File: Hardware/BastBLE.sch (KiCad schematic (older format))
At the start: 33 parts

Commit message: assigned pinout complete
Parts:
- U2: renamed from U?; symbol electroniccats:E73-2G4M08S1C -> BastBLE-rescue:E73-2G4M08S1C-electroniccats
- gave numbers to parts that had none: 32
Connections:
- net labels removed: BOOT, DFU, SWDCLK
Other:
- note added: "NOTA: BOOT"
- note added: "NOTA: DFU??"

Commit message: SWD pinout ok, assigned mosfet
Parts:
- removed Q1: BS870, Package_TO_SOT_SMD:SOT-23, symbol Transistor_FET:BS870
- added Q?: DMG3415U-7, symbol Device:Q_PMOS_SGD
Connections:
- wire segments 173 -> 172
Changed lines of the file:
@@
-$EndComp
-$Comp
-L Transistor_FET:BS870 Q1
-U 1 1 5E1F28D4
-P 1190 5640
-F 0 "Q1" H 1396 5686 50  0000 L CNN
-F 1 "BS870" H 1396 5595 50  0000 L CNN
-F 2 "Package_TO_SOT_SMD:SOT-23" H 1390 5565 50  0001 L CIN
-F 3 "http://www.diodes.com/assets/Datasheets/ds11302.pdf" H 1190 5640 50  0001 L CNN
-	1    1190 5640
-	1    0    0    -1
 $EndComp
 $Comp
@@
 Wire Wire Line
 	6190 5690 6120 5690
+Text Label 6115 5490 2    50   ~ 0
+SWDIO
 Text Label 6120 5590 2    50   ~ 0
-SWDIO
-Text Label 6120 5690 2    50   ~ 0
 SWCLK
 $Comp
 L power:GND #PWR029
 U 1 1 5E237980
-P 5810 5565
-F 0 "#PWR029" H 5810 5315 50  0001 C CNN
-F 1 "GND" H 5815 5392 50  0000 C CNN
-F 2 "" H 5810 5565 50  0001 C CNN
-F 3 "" H 5810 5565 50  0001 C CNN
-	1    5810 5565
+P 6120 5690
+F 0 "#PWR029" H 6120 5440 50  0001 C CNN
+F 1 "GND" H 6125 5517 50  0000 C CNN
+F 2 "" H 6120 5690 50  0001 C CNN
+F 3 "" H 6120 5690 50  0001 C CNN
+	1    6120 5690
 	1    0    0    -1
 $EndComp
@@
 	1    0    0    -1
 $EndComp
-Wire Wire Line
-	5810 5490 5810 5565
-Wire Wire Line
-	5810 5490 6190 5490
 Wire Notes Line
 	6975 6530 6975 4335
@@
 Text Notes 1195 3160 0    50   ~ 0
 NOTA: BOOT
+Wire Wire Line
+	6190 5490 6115 5490
+$Comp
+L Device:Q_PMOS_SGD Q?
+U 1 1 5E39C807
+P 1190 5640
+F 0 "Q?" H 1394 5686 50  0000 L CNN
+F 1 "DMG3415U-7" H 1370 5770 50  0000 L CNN
+F 2 "" H 1390 5740 50  0001 C CNN
+F 3 "~" H 1190 5640 50  0001 C CNN
+	1    1190 5640
+	1    0    0    -1
+$EndComp
 $EndSCHEMATC

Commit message: Format adafruit in PCB, init BOM
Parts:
- C1, C2, C3, C4, C5, C6, C7, C8: footprint (none) -> Capacitor_SMD:C_0603_1608Metric_Pad1.05x0.95mm_HandSolder
- D1: footprint Diode_THT:D_DO-201AD_P15.24mm_Horizontal -> Diode_SMD:D_SOD-123F
- D2, D3: footprint (none) -> LED_SMD:LED_0603_1608Metric_Pad1.05x0.95mm_HandSolder
- R1, R2, R3, R4, R5, R6, R7, R8, R9: footprint (none) -> Resistor_SMD:R_0603_1608Metric_Pad1.05x0.95mm_HandSolder
- gave numbers to parts that had none: 1
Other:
- moved on the sheet: J4, L1, Y1

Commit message: init assignament footprints
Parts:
- J2: footprint (none) -> Connector_PinSocket_2.54mm:PinSocket_1x04_P2.54mm_Vertical
- J3: footprint (none) -> Connector_PinHeader_2.54mm:PinHeader_1x16_P2.54mm_Vertical
- J4: footprint (none) -> Connector_PinHeader_2.54mm:PinHeader_1x12_P2.54mm_Vertical
- L1: footprint (none) -> Connector_PinHeader_2.54mm:PinHeader_2x01_P2.54mm_Vertical_SMD
- P1: footprint (none) -> Connectors_ElectronicCats:C393939
- Q1: footprint (none) -> Package_TO_SOT_SMD:SOT-23_Handsoldering
- SW1: footprint (none) -> Button_Switch_SMD:SW_SPST_TL3342
- U2: footprint (none) -> Rf:E73-2G4M08S1C-52840
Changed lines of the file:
@@
 F 0 "U2" H 2220 3290 50  0000 C CNN
 F 1 "E73-2G4M08S1C" H 2220 3199 50  0000 C CNN
-F 2 "" H 2245 1925 50  0001 C CNN
+F 2 "Rf:E73-2G4M08S1C-52840" H 2245 1925 50  0001 C CNN
 F 3 "" H 2245 1925 50  0001 C CNN
 	1    2245 1925
@@
 F 0 "L1" V 3165 2605 50  0000 C CNN
 F 1 "10uH" V 3070 2735 50  0000 C CNN
-F 2 "" H 3120 2725 50  0001 C CNN
+F 2 "Connector_PinHeader_2.54mm:PinHeader_2x01_P2.54mm_Vertical_SMD" H 3120 2725 50  0001 C CNN
 F 3 "~" H 3120 2725 50  0001 C CNN
 	1    3120 2725
@@
 F 0 "J4" H 10000 1902 50  0000 L CNN
 F 1 "Conn_right" V 10035 1390 50  0000 L CNN
-F 2 "" H 9920 1910 50  0001 C CNN
+F 2 "Connector_PinHeader_2.54mm:PinHeader_1x12_P2.54mm_Vertical" H 9920 1910 50  0001 C CNN
 F 3 "~" H 9920 1910 50  0001 C CNN
 	1    9920 1910
@@
 F 0 "J3" H 9223 1090 50  0000 C CNN
 F 1 "Conn_left" V 9410 2125 50  0000 C CNN
-F 2 "" H 9305 2115 50  0001 C CNN
+F 2 "Connector_PinHeader_2.54mm:PinHeader_1x16_P2.54mm_Vertical" H 9305 2115 50  0001 C CNN
 F 3 "~" H 9305 2115 50  0001 C CNN
 	1    9305 2115
@@
 F 0 "P1" H 5242 3987 50  0000 C CNN
 F 1 "USB_C_Plug_USB2.0" H 5242 3896 50  0000 C CNN
-F 2 "" H 5285 3120 50  0001 C CNN
+F 2 "Connectors_ElectronicCats:C393939" H 5285 3120 50  0001 C CNN
 F 3 "https://www.usb.org/sites/default/files/documents/usb_type-c.zip" H 5285 3120 50  0001 C CNN
 	1    5135 3120
@@
 F 0 "SW1" H 7380 1380 50  0000 C CNN
 F 1 "RESET" H 7380 1289 50  0000 C CNN
-F 2 "" H 7380 1295 50  0001 C CNN
-F 3 "~" H 7380 1295 50  0001 C CNN
+F 2 "Button_Switch_SMD:SW_SPST_TL3342" H 7380 1295 50  0001 C CNN
+F 3 "TS-1185EC-C-D-B" H 7380 1295 50  0001 C CNN
 	1    7380 1095
 	1    0    0    -1
@@
 F 0 "J2" H 6470 5482 50  0000 L CNN
 F 1 "SWD" H 6470 5391 50  0000 L CNN
-F 2 "" H 6390 5490 50  0001 C CNN
+F 2 "Connector_PinSocket_2.54mm:PinSocket_1x04_P2.54mm_Vertical" H 6390 5490 50  0001 C CNN
 F 3 "~" H 6390 5490 50  0001 C CNN
 	1    6390 5490
@@
 F 0 "Q1" H 1394 5686 50  0000 L CNN
 F 1 "DMG3415U-7" H 1370 5770 50  0000 L CNN
-F 2 "" H 1390 5740 50  0001 C CNN
+F 2 "Package_TO_SOT_SMD:SOT-23_Handsoldering" H 1390 5740 50  0001 C CNN
 F 3 "~" H 1190 5640 50  0001 C CNN
 	1    1190 5640

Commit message: Review PCB
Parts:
- U2: symbol BastBLE-rescue:E73-2G4M08S1C-electroniccats -> BastBLE-rescue:E73-2G4M08S1C-electroniccats-BastBLE-rescue
- Y1: footprint (none) -> Crystal:Crystal_SMD_SeikoEpson_MC146-4Pin_6.7x1.5mm
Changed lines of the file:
@@
 $EndDescr
 $Comp
-L BastBLE-rescue:E73-2G4M08S1C-electroniccats U2
+L BastBLE-rescue:E73-2G4M08S1C-electroniccats-BastBLE-rescue U2
 U 1 1 5E1E9971
 P 2245 1925
@@
 F 3 "" H 2245 1925 50  0001 C CNN
 	1    2245 1925
-	1    0    0    -1
-$EndComp
-$Comp
-L Battery_Management:MCP73831-2-OT U3
-U 1 1 5E1EEE26
-P 4270 5305
-F 0 "U3" H 4385 5550 50  0000 C CNN
-F 1 "MCP73831-2-OT" H 3880 5545 50  0000 C CNN
-F 2 "Package_TO_SOT_SMD:SOT-23-5" H 4320 5055 50  0001 L CIN
-F 3 "http://ww1.microchip.com/downloads/en/DeviceDoc/20001984g.pdf" H 4120 5255 50  0001 C CNN
-	1    4270 5305
 	1    0    0    -1
 $EndComp
@@
 F 0 "Y1" V 1110 1730 50  0000 L CNN
 F 1 "32Khz" V 1195 1650 50  0000 L CNN
-F 2 "" H 1200 1955 50  0001 C CNN
+F 2 "Crystal:Crystal_SMD_SeikoEpson_MC146-4Pin_6.7x1.5mm" H 1200 1955 50  0001 C CNN
 F 3 "~" H 1200 1955 50  0001 C CNN
 	1    1200 1955
@@
 $EndComp
 Wire Wire Line
-	4270 5005 4270 4920
-Wire Wire Line
-	4270 5605 4270 5640
-$Comp
-L power:GND #PWR017
-U 1 1 5E25A527
-P 4270 5675
-F 0 "#PWR017" H 4270 5425 50  0001 C CNN
-F 1 "GND" H 4275 5502 50  0000 C CNN
-F 2 "" H 4270 5675 50  0001 C CNN
-F 3 "" H 4270 5675 50  0001 C CNN
-	1    4270 5675
-	1    0    0    -1
-$EndComp
-Wire Wire Line
-	4670 5205 4745 5205
-Wire Wire Line
-	4670 5405 4740 5405
-Wire Wire Line
-	3870 5405 3745 5405
-$Comp
-L Device:LED D3
-U 1 1 5E2607F0
-P 5185 5405
-F 0 "D3" H 5178 5621 50  0000 C CNN
-F 1 "LED" H 5178 5530 50  0000 C CNN
-F 2 "LED_SMD:LED_0603_1608Metric_Pad1.05x0.95mm_HandSolder" H 5185 5405 50  0001 C CNN
-F 3 "~" H 5185 5405 50  0001 C CNN
-	1    5185 5405
-	1    0    0    -1
-$EndComp
-$Comp
-L Device:R_Small R7
-U 1 1 5E260E7D
-P 4840 5405
-F 0 "R7" V 4765 5405 50  0000 C CNN
-F 1 "1K" V 4920 5400 50  0000 C CNN
-F 2 "Resistor_SMD:R_0603_1608Metric_Pad1.05x0.95mm_HandSolder" H 4840 5405 50  0001 C CNN
-F 3 "~" H 4840 5405 50  0001 C CNN
-	1    4840 5405
-	0    1    1    0
-$EndComp
-Wire Wire Line
-	4940 5405 5035 5405
-Wire Wire Line
-	5335 5405 5415 5405
-Wire Wire Line
 	5415 5405 5415 5375
-$Comp
-L power:+BATT #PWR022
-U 1 1 5E26906E
-P 4915 5205
-F 0 "#PWR022" H 4915 5055 50  0001 C CNN
-F 1 "+BATT" H 4930 5378 50  0000 C CNN
-F 2 "" H 4915 5205 50  0001 C CNN
-F 3 "" H 4915 5205 50  0001 C CNN
-	1    4915 5205
-	1    0    0    -1
-$EndComp
-$Comp
-L Device:R_Small R3
-U 1 1 5E26C7D7
-P 3745 5505
-F 0 "R3" H 3804 5551 50  0000 L CNN
-F 1 "4K7" H 3804 5460 50  0000 L CNN
-F 2 "Resistor_SMD:R_0603_1608Metric_Pad1.05x0.95mm_HandSolder" H 3745 5505 50  0001 C CNN
-F 3 "~" H 3745 5505 50  0001 C CNN
-	1    3745 5505
-	1    0    0    -1
-$EndComp
-Wire Wire Line
-	3745 5605 3745 5640
-Wire Wire Line
-	3745 5640 4270 5640
-Connection ~ 4270 5640
-Wire Wire Line
-	4270 5640 4270 5675
-$Comp
-L Device:C_Small C3
-U 1 1 5E26FE7B
-P 4745 5035
-F 0 "C3" H 4610 5165 50  0000 L CNN
-F 1 "10uF" H 4510 5100 50  0000 L CNN
-F 2 "Capacitor_SMD:C_0603_1608Metric_Pad1.05x0.95mm_HandSolder" H 4745 5035 50  0001 C CNN
-F 3 "~" H 4745 5035 50  0001 C CNN
-	1    4745 5035
-	1    0    0    -1
-$EndComp
-Wire Wire Line
-	4745 5135 4745 5205
-Connection ~ 4745 5205
-Wire Wire Line
-	4745 5205 4915 5205
-Wire Wire Line
-	4745 4935 4745 4635
 Wire Wire Line
 	4745 4635 4830 4635
-Wire Wire Line
-	4830 4635 4830 4675
-$Comp
-L power:GND #PWR021
-U 1 1 5E275216
-P 4830 4675
-F 0 "#PWR021" H 4830 4425 50  0001 C CNN
-F 1 "GND" H 4835 4502 50  0000 C CNN
-F 2 "" H 4830 4675 50  0001 C CNN
-F 3 "" H 4830 4675 50  0001 C CNN
-	1    4830 4675
-	1    0    0    -1
-$EndComp
 $Comp
 L Connector:Screw_Terminal_01x02 J1
@@
 EN
 $Comp
-L power:VBUS #PWR016
-U 1 1 5E3A4B4E
-P 4270 4920
-F 0 "#PWR016" H 4270 4770 50  0001 C CNN
-F 1 "VBUS" H 4285 5093 50  0000 C CNN
-F 2 "" H 4270 4920 50  0001 C CNN
-F 3 "" H 4270 4920 50  0001 C CNN
-	1    4270 4920
-	1    0    0    -1
-$EndComp
-$Comp
-L power:VBUS #PWR026
-U 1 1 5E3A5E21
-P 5415 5375
-F 0 "#PWR026" H 5415 5225 50  0001 C CNN
-F 1 "VBUS" H 5430 5548 50  0000 C CNN
-F 2 "" H 5415 5375 50  0001 C CNN
-F 3 "" H 5415 5375 50  0001 C CNN
-	1    5415 5375
-	1    0    0    -1
-$EndComp
-$Comp
 L Device:R_Small R5
 U 1 1 5E3AF686
@@
 	1    0    0    -1
 $EndComp
+$Comp
+L power:VBUS #PWR026
+U 1 1 5E3A5E21
+P 5415 5375
+F 0 "#PWR026" H 5415 5225 50  0001 C CNN
+F 1 "VBUS" H 5430 5548 50  0000 C CNN
+F 2 "" H 5415 5375 50  0001 C CNN
+F 3 "" H 5415 5375 50  0001 C CNN
+	1    5415 5375
+	1    0    0    -1
+$EndComp
+$Comp
+L power:VBUS #PWR016
+U 1 1 5E3A4B4E
+P 4270 4920
+F 0 "#PWR016" H 4270 4770 50  0001 C CNN
+F 1 "VBUS" H 4285 5093 50  0000 C CNN
+F 2 "" H 4270 4920 50  0001 C CNN
+F 3 "" H 4270 4920 50  0001 C CNN
+	1    4270 4920
+	1    0    0    -1
+$EndComp
+$Comp
+L power:GND #PWR021
+U 1 1 5E275216
+P 4830 4675
+F 0 "#PWR021" H 4830 4425 50  0001 C CNN
+F 1 "GND" H 4835 4502 50  0000 C CNN
+F 2 "" H 4830 4675 50  0001 C CNN
+F 3 "" H 4830 4675 50  0001 C CNN
+	1    4830 4675
+	1    0    0    -1
+$EndComp
+Wire Wire Line
+	4830 4635 4830 4675
+Wire Wire Line
+	4745 4935 4745 4635
+Wire Wire Line
+	4745 5205 4915 5205
+Connection ~ 4745 5205
+Wire Wire Line
+	4745 5135 4745 5205
+$Comp
+L Device:C_Small C3
+U 1 1 5E26FE7B
+P 4745 5035
+F 0 "C3" H 4610 5165 50  0000 L CNN
+F 1 "10uF" H 4510 5100 50  0000 L CNN
+F 2 "Capacitor_SMD:C_0603_1608Metric_Pad1.05x0.95mm_HandSolder" H 4745 5035 50  0001 C CNN
+F 3 "~" H 4745 5035 50  0001 C CNN
+	1    4745 5035
+	1    0    0    -1
+$EndComp
+Wire Wire Line
+	4270 5640 4270 5675
+Connection ~ 4270 5640
+Wire Wire Line
+	3745 5640 4270 5640
+Wire Wire Line
+	3745 5605 3745 5640
+$Comp
+L Device:R_Small R3
+U 1 1 5E26C7D7
+P 3745 5505
+F 0 "R3" H 3804 5551 50  0000 L CNN
+F 1 "4K7" H 3804 5460 50  0000 L CNN
+F 2 "Resistor_SMD:R_0603_1608Metric_Pad1.05x0.95mm_HandSolder" H 3745 5505 50  0001 C CNN
+F 3 "~" H 3745 5505 50  0001 C CNN
+	1    3745 5505
+	1    0    0    -1
+$EndComp
+$Comp
+L power:+BATT #PWR022
+U 1 1 5E26906E
+P 4915 5205
+F 0 "#PWR022" H 4915 5055 50  0001 C CNN
+F 1 "+BATT" H 4930 5378 50  0000 C CNN
+F 2 "" H 4915 5205 50  0001 C CNN
+F 3 "" H 4915 5205 50  0001 C CNN
+	1    4915 5205
+	1    0    0    -1
+$EndComp
+Wire Wire Line
+	5335 5405 5415 5405
+Wire Wire Line
+	4940 5405 5035 5405
+$Comp
+L Device:R_Small R7
+U 1 1 5E260E7D
+P 4840 5405
+F 0 "R7" V 4765 5405 50  0000 C CNN
+F 1 "1K" V 4920 5400 50  0000 C CNN
+F 2 "Resistor_SMD:R_0603_1608Metric_Pad1.05x0.95mm_HandSolder" H 4840 5405 50  0001 C CNN
+F 3 "~" H 4840 5405 50  0001 C CNN
+	1    4840 5405
+	0    1    1    0
+$EndComp
+$Comp
+L Device:LED D3
+U 1 1 5E2607F0
+P 5185 5405
+F 0 "D3" H 5178 5621 50  0000 C CNN
+F 1 "LED" H 5178 5530 50  0000 C CNN
+F 2 "LED_SMD:LED_0603_1608Metric_Pad1.05x0.95mm_HandSolder" H 5185 5405 50  0001 C CNN
+F 3 "~" H 5185 5405 50  0001 C CNN
+	1    5185 5405
+	1    0    0    -1
+$EndComp
+Wire Wire Line
+	3870 5405 3745 5405
+Wire Wire Line
+	4670 5405 4740 5405
+Wire Wire Line
+	4670 5205 4745 5205
+$Comp
+L power:GND #PWR017
+U 1 1 5E25A527
+P 4270 5675
+F 0 "#PWR017" H 4270 5425 50  0001 C CNN
+F 1 "GND" H 4275 5502 50  0000 C CNN
+F 2 "" H 4270 5675 50  0001 C CNN
+F 3 "" H 4270 5675 50  0001 C CNN
+	1    4270 5675
+	1    0    0    -1
+$EndComp
+Wire Wire Line
+	4270 5605 4270 5640
+Wire Wire Line
+	4270 5005 4270 4920
+$Comp
+L Battery_Management:MCP73831-2-OT U3
+U 1 1 5E1EEE26
+P 4270 5305
+F 0 "U3" H 4385 5550 50  0000 C CNN
+F 1 "MCP73831-2-OT" H 3880 5545 50  0000 C CNN
+F 2 "Package_TO_SOT_SMD:SOT-23-5" H 4320 5055 50  0001 L CIN
+F 3 "http://ww1.microchip.com/downloads/en/DeviceDoc/20001984g.pdf" H 4120 5255 50  0001 C CNN
+	1    4270 5305
+	1    0    0    -1
+$EndComp

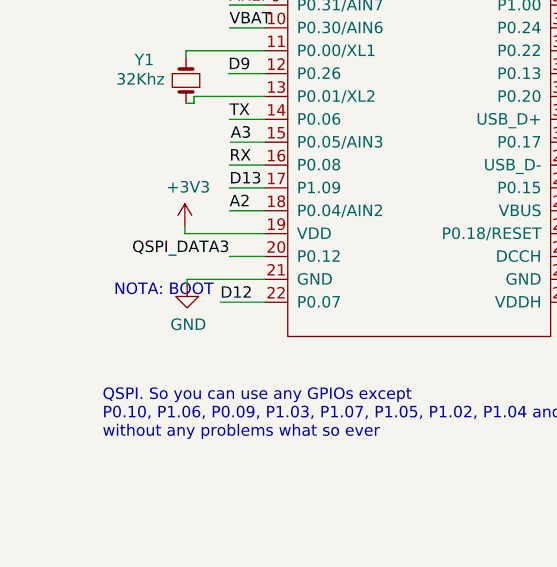
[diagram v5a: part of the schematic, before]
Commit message: change L1 package
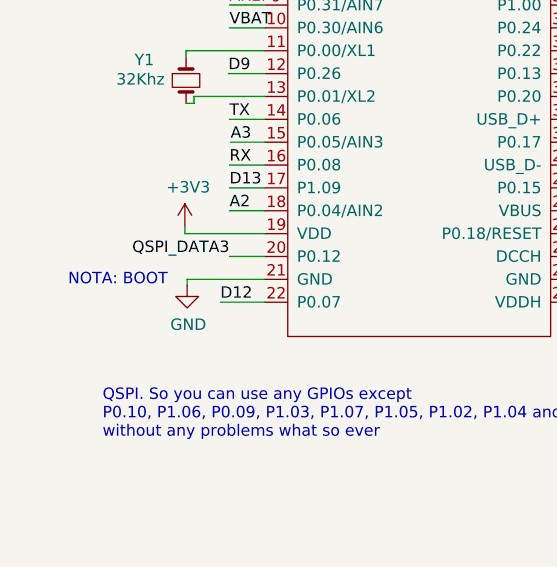
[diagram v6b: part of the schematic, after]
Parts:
- L1: footprint Connector_PinHeader_2.54mm:PinHeader_2x01_P2.54mm_Vertical_SMD -> Inductor_SMD:L_0603_1608Metric_Pad1.05x0.95mm_HandSolder
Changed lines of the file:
@@
 F 0 "L1" V 3165 2605 50  0000 C CNN
 F 1 "10uH" V 3070 2735 50  0000 C CNN
-F 2 "Connector_PinHeader_2.54mm:PinHeader_2x01_P2.54mm_Vertical_SMD" H 3120 2725 50  0001 C CNN
+F 2 "Inductor_SMD:L_0603_1608Metric_Pad1.05x0.95mm_HandSolder" H 3120 2725 50  0001 C CNN
 F 3 "~" H 3120 2725 50  0001 C CNN
 	1    3120 2725
@@
 Text Notes 3205 1420 0    50   ~ 0
 NOTA: DFU??
-Text Notes 885  2905 0    50   ~ 0
+Text Notes 684  2858 0    50   ~ 0
 NOTA: BOOT
 Wire Wire Line

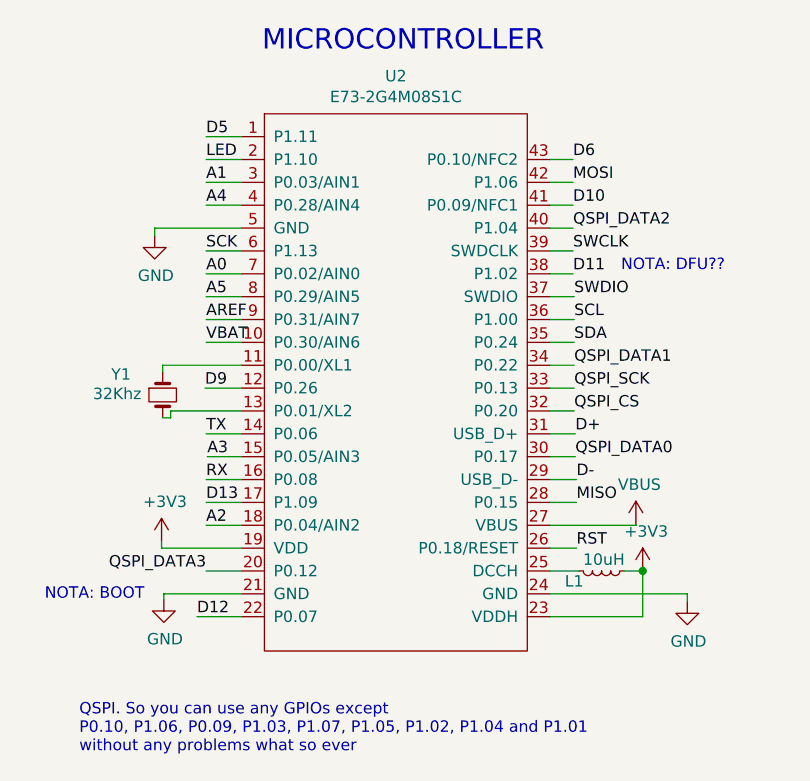
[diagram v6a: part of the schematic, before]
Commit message: change pins schematic
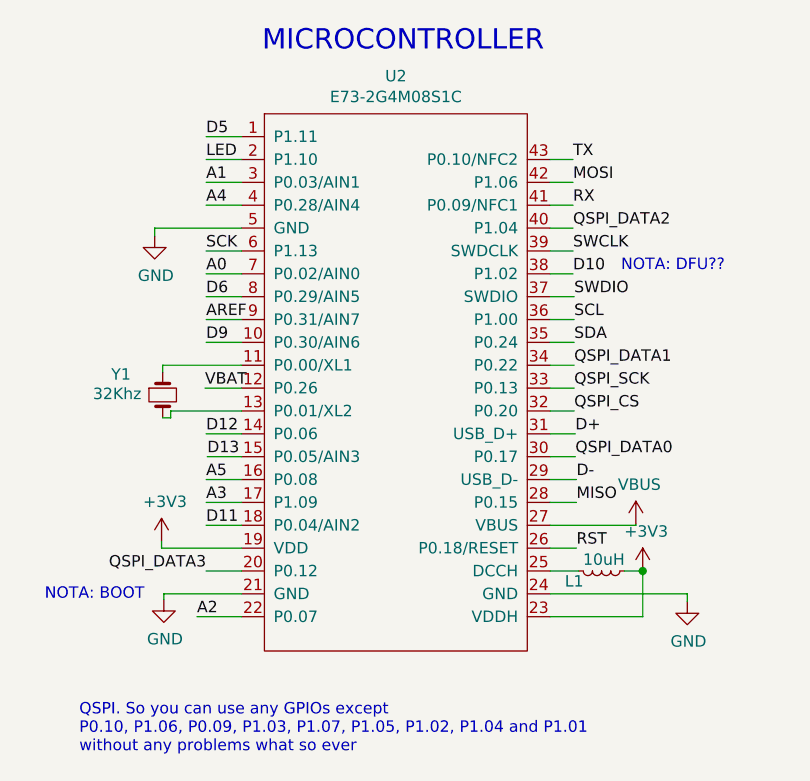
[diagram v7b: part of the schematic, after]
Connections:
- net A2: now also U2.22 (P0.07); no longer U2.18 (P0.04/AIN2)
- net A3: now also U2.17 (P1.09); no longer U2.15 (P0.05/AIN3)
- net A5: now also U2.16 (P0.08); no longer U2.8 (P0.29/AIN5)
- net D10: now also U2.38 (P1.02); no longer U2.41 (P0.09/NFC1)
- net D11: now also U2.18 (P0.04/AIN2); no longer U2.38 (P1.02)
- net D12: now also U2.14 (P0.06); no longer U2.22 (P0.07)
- net D13: now also U2.15 (P0.05/AIN3); no longer U2.17 (P1.09)
- net D6: now also U2.8 (P0.29/AIN5); no longer U2.43 (P0.10/NFC2)
- net D9: now also U2.10 (P0.30/AIN6); no longer U2.12 (P0.26)
- net RX: now also U2.41 (P0.09/NFC1); no longer U2.16 (P0.08)
- net TX: now also U2.43 (P0.10/NFC2); no longer U2.14 (P0.06)
- net VBAT: now also U2.12 (P0.26); no longer U2.10 (P0.30/AIN6)
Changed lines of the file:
@@
 EESchema Schematic File Version 4
+LIBS:BastBLE-cache
 EELAYER 30 0
 EELAYER END
@@
 	1    0    0    -1
 $EndComp
-Wire Wire Line
-	1195 2625 1195 2595
-Wire Wire Line
-	1195 2625 1545 2625
-$Comp
-L power:+3V3 #PWR06
-U 1 1 5E20EBA3
-P 1195 2595
-F 0 "#PWR06" H 1195 2445 50  0001 C CNN
-F 1 "+3V3" H 1210 2768 50  0000 C CNN
-F 2 "" H 1195 2595 50  0001 C CNN
-F 3 "" H 1195 2595 50  0001 C CNN
-	1    1195 2595
-	1    0    0    -1
-$EndComp
-Text Label 2995 1325 0    50   ~ 0
-SWCLK
 Text Label 3000 1525 0    50   ~ 0
 SWDIO
@@
 Text Label 1390 925  0    50   ~ 0
 LED
-Text Label 1390 2325 0    50   ~ 0
+Text Label 2995 1125 0    50   ~ 0
 RX
-Text Label 1350 2925 0    50   ~ 0
+Text Label 1390 2125 0    50   ~ 0
 D12
 Wire Wire Line
@@
 Text Label 1390 1025 0    50   ~ 0
 A1
-Text Label 1390 2525 0    50   ~ 0
-A2
-Text Label 1395 2225 0    50   ~ 0
+Text Label 1390 2425 0    50   ~ 0
 A3
 Text Label 1390 1125 0    50   ~ 0
 A4
-Text Label 1390 1525 0    50   ~ 0
+Text Label 1390 2325 0    50   ~ 0
 A5
 Text Label 1390 1625 0    50   ~ 0
@@
 	3300 2925 2895 2925
 Connection ~ 3300 2725
-Text Label 1390 2125 0    50   ~ 0
+Text Label 2995 925  0    50   ~ 0
 TX
-Text Label 1390 2425 0    50   ~ 0
-D13
-Text Label 1385 1925 0    50   ~ 0
+Text Label 1390 1725 0    50   ~ 0
 D9
 Text Label 3005 2225 0    50   ~ 0
@@
 Wire Wire Line
 	4720 6855 4720 6795
-Text Label 1390 1725 0    50   ~ 0
+Text Label 1385 1925 0    50   ~ 0
 VBAT
 Text Label 4905 6855 0    50   ~ 0
@@
 Text Label 1390 825  0    50   ~ 0
 D5
-Text Label 2995 925  0    50   ~ 0
+Text Label 1390 1525 0    50   ~ 0
 D6
-Text Label 2995 1125 0    50   ~ 0
+Text Label 2995 1425 0    50   ~ 0
 D10
-Text Label 2995 1425 0    50   ~ 0
-D11
 Text Notes 3205 1420 0    50   ~ 0
 NOTA: DFU??
@@
 	1    0    0    -1
 $EndComp
+Wire Wire Line
+	1195 2625 1545 2625
+Wire Wire Line
+	1195 2625 1195 2595
+$Comp
+L power:+3V3 #PWR06
+U 1 1 5E20EBA3
+P 1195 2595
+F 0 "#PWR06" H 1195 2445 50  0001 C CNN
+F 1 "+3V3" H 1210 2768 50  0000 C CNN
+F 2 "" H 1195 2595 50  0001 C CNN
+F 3 "" H 1195 2595 50  0001 C CNN
+	1    1195 2595
+	1    0    0    -1
+$EndComp
+Text Label 1395 2225 0    50   ~ 0
+D13
+Text Label 2995 1325 0    50   ~ 0
+SWCLK
+Text Label 1390 2525 0    50   ~ 0
+D11
+Text Label 1350 2925 0    50   ~ 0
+A2
 $EndSCHEMATC

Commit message: erase traces, add note
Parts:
- Q1: footprint Package_TO_SOT_SMD:SOT-23_Handsoldering -> Package_TO_SOT_SMD:SOT-23
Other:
- note added: "Agregar capacitores"
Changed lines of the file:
@@
 EESchema Schematic File Version 4
-LIBS:BastBLE-cache
 EELAYER 30 0
 EELAYER END
@@
 F 0 "Q1" H 1394 5686 50  0000 L CNN
 F 1 "DMG3415U-7" H 1370 5770 50  0000 L CNN
-F 2 "Package_TO_SOT_SMD:SOT-23_Handsoldering" H 1390 5740 50  0001 C CNN
+F 2 "Package_TO_SOT_SMD:SOT-23" H 1390 5740 50  0001 C CNN
 F 3 "~" H 1190 5640 50  0001 C CNN
 	1    1190 5640
@@
 Text Label 1350 2925 0    50   ~ 0
 A2
+Text Notes 575  2230 0    50   Italic 10
+Agregar capacitores
 $EndSCHEMATC
